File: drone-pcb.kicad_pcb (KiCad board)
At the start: 2 copper layers, 65 x 48.5 mm, 46 parts, among them J1 Conn_01x02_Pin, J10 Conn_01x03_Pin, J11 Conn_01x03_Pin, J12 Conn_01x03_Pin, J2 Conn_01x02_Pin, J3 Conn_01x02_Pin, J4 Conn_01x02_Pin, J5 Conn_01x02_Pin, J6 Conn_01x02_Pin, J7 USB_C_Receptacle_USB2.0_16P, J8 Conn_01x02_Pin, J9 Conn_01x03_Pin, Q1 AO3400A, Q2 AO3400A, Q3 AO3400A, Q4 AO3400A, Q5 AO3400A, Q6 AO3400A, SW1 CK_KMS2xxGP, U1 STM32F030C8Tx, U2 nRF24L01P, U3 MCP73831-2-OT, U4 TLV75533PDBV

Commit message: test export after makefile genaralisation
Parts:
- added U5: MPU-6050, Sensor_Motion:InvenSense_QFN-24_4x4mm_P0.5mm, F.Cu at (142.2, 120.7)
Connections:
- J8 pad 1: /battery+ -> /Vmotor
- R11 pad 1: /m1 -> Net-(Q1-G)
- R12 pad 1: /m2 -> Net-(Q2-G)
- R13 pad 1: /m3 -> Net-(Q3-G)
- R14 pad 1: /m4 -> Net-(Q4-G)
- R15 pad 1: /m5 -> Net-(Q5-G)
- R16 pad 1: /m6 -> Net-(Q6-G)
- U3 pad 3: /battery+ -> /Vmotor
- U4 pad 1: /battery+ -> /Vmotor
- U4 pad 3: /battery+ -> /Vmotor

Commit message: start placing footprints
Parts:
- moved SW1 80.0 mm to (147.6, 42.9)
- moved R13 79.5 mm to (114.6, 34.8)
- moved R12 79.5 mm to (114.6, 31.9)
- moved J3 78.3 mm to (81.6, 45.1), turned to -135 degrees
- moved Q6 77.1 mm to (198.3, 86.2)
- moved R7 76.3 mm to (189.0, 61.6)
- moved J2 69.8 mm to (69.1, 85.8), turned to -90 degrees
- moved Q3 65.9 mm to (89.5, 52.5)
- moved J8 65.0 mm to (102.0, 107.9)
- moved U3 63.8 mm to (111.9, 102.8)
- moved R6 63.5 mm to (191.2, 84.7)
- moved R3 60.1 mm to (96.9, 54.1)
- moved R17 59.7 mm to (161.5, 45.2)
- moved R8 57.7 mm to (188.1, 67.4), turned to 180 degrees
- moved Q4 56.9 mm to (185.2, 114.2)
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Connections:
- U5 pad 1: unconnected-(U5-CLKIN-Pad1) -> GND
- U5 pad 12: unconnected-(U5-INT-Pad12) -> /imu_INT
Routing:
- added copper zone on B.Cu, net GND
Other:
- board outline removed

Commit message: half done
placed chips, not routed, schematic incomplete
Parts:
- removed C4: C, Capacitor_SMD:C_0805_2012Metric_Pad1.18x1.45mm_HandSolder
- removed J11, J12: Conn_01x03_Pin, Connector_PinHeader_2.54mm:PinHeader_1x03_P2.54mm_Vertical
- removed R16: 100k, Resistor_SMD:R_0805_2012Metric_Pad1.20x1.40mm_HandSolder
- removed R17, R18: 10k, Resistor_SMD:R_0805_2012Metric_Pad1.20x1.40mm_HandSolder
- removed R7, R8: 27, Resistor_SMD:R_0805_2012Metric_Pad1.20x1.40mm_HandSolder
- removed SW1: CK_KMS2xxGP, Button_Switch_SMD:SW_SPST_CK_KMS2xxGP
- added D2: LED, LED_SMD:LED_0805_2012Metric_Pad1.15x1.40mm_HandSolder, F.Cu at (203.7, 101.7)
- added REF**: MountingHole_3.2mm_M3_ISO7380, MountingHole:MountingHole_3.2mm_M3_ISO7380, F.Cu at (239.3, 74.9)
- added REF**: MountingHole_3.2mm_M3_ISO7380, MountingHole:MountingHole_3.2mm_M3_ISO7380, F.Cu at (239.2, 105.7)
- added REF**: MountingHole_3.2mm_M3_ISO7380, MountingHole:MountingHole_3.2mm_M3_ISO7380, F.Cu at (205.3, 75.0)
- added REF**: MountingHole_3.2mm_M3_ISO7380, MountingHole:MountingHole_3.2mm_M3_ISO7380, F.Cu at (205.2, 105.7)
- added SW2: SW_Push_Dual_x2, ch32-devBoard-symbols:smd-push-button-TS3425PA, F.Cu at (239.3, 80.1)
- added U6: DW01A, Package_TO_SOT_SMD:SOT-23-6, F.Cu at (204.8, 81.0)
- C1, C2, C3, Q1, Q2, Q3, Q4, Q5, Q6, R11, R12, R3, R4, R5, R6: moved to B.Cu
- J5: value Conn_01x02_Pin -> USB_C_Receptacle_USB2.0_16P; footprint Connector_JST:JST_XH_S2B-XH-A-1_1x02_P2.50mm_Horizontal -> Connector_USB:USB_C_Receptacle_HCTL_HC-TYPE-C-16P-01A
- J6: footprint Connector_JST:JST_XH_S2B-XH-A-1_1x02_P2.50mm_Horizontal -> Connector_JST:JST_XH_B2B-XH-A_1x02_P2.50mm_Vertical
- J7: value USB_C_Receptacle_USB2.0_16P -> Conn_01x03_Pin; footprint Connector_USB:USB_C_Receptacle_HCTL_HC-TYPE-C-16P-01A -> Connector_PinHeader_2.54mm:PinHeader_1x03_P2.54mm_Vertical
- J8: value Conn_01x02_Pin -> Conn_01x03_Pin; footprint Connector_JST:JST_XH_B2B-XH-A_1x02_P2.50mm_Vertical -> Connector_PinHeader_2.54mm:PinHeader_1x03_P2.54mm_Vertical
- R1, R2: value 100R -> 5.1k; moved to B.Cu
- R10, R9: value 4.7k -> 100k; moved to B.Cu
- R13, R14, R15: value 100k -> 10k
- U1: value STM32F030C8Tx -> STM32F103C8Tx
- U2: value nRF24L01P -> TLV75533PDBV; footprint Package_DFN_QFN:QFN-20-1EP_4x4mm_P0.5mm_EP2.5x2.5mm -> Package_TO_SOT_SMD:SOT-23-5
- U3: value MCP73831-2-OT -> MPU-9250; footprint Package_TO_SOT_SMD:SOT-23-5 -> Sensor_Motion:InvenSense_QFN-24_3x3mm_P0.4mm
- U4: value TLV75533PDBV -> MCP73831-2-OT
- U5: value MPU-6050 -> nRF24L01P; footprint Sensor_Motion:InvenSense_QFN-24_4x4mm_P0.5mm -> Package_DFN_QFN:QFN-20-1EP_4x4mm_P0.5mm_EP2.5x2.5mm
- moved J2 171.3 mm to (240.3, 90.2), turned to 90 degrees
- moved Q2 161.3 mm to (236.4, 86.8), turned to 0 degrees
- moved Q3 147.1 mm to (228.2, 101.7), turned to -90 degrees
- moved R2 133.3 mm to (214.5, 105.2), turned to -90 degrees
- moved J9 132.3 mm to (240.4, 95.2)
- moved J8 130.7 mm to (232.6, 101.9)
- moved J3 130.2 mm to (204.0, 89.6), turned to -90 degrees
- moved R3 129.5 mm to (224.3, 77.3), turned to -90 degrees
- moved J10 124.0 mm to (236.7, 95.2)
- moved U3 118.3 mm to (229.7, 91.6)
- moved R13 113.2 mm to (208.3, 98.3)
- moved R11 112.8 mm to (225.4, 101.3), turned to 90 degrees
- moved R12 110.2 mm to (208.0, 90.3)
- moved U5 106.3 mm to (229.7, 82.8)
- moved R1 96.0 mm to (211.0, 105.3)
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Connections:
- J1 pad 1: /Vmotor -> /Vbat
- J10 pad 1: +3V3 -> /swdio
- J10 pad 2: /boot1 -> /swdclk
- J2 pad 1: /Vmotor -> /Vbat
- J3 pad 1: /Vmotor -> /Vbat
- J3 pad 2: /g3 -> /g4
- J4 pad 1: /Vmotor -> /Vbat
- J4 pad 2: /g4 -> /g3
- J6 pad 1: /Vmotor -> /battery+
- J6 pad 2: /g6 -> GND
- J8 pad 1: /Vmotor -> +3V3
- J8 pad 2: GND -> /boot1
- J9 pad 1: +3V3 -> /uart_tx
- J9 pad 2: /boot0 -> /uart_rx
- Q5 pad 1: Net-(Q5-G) -> /charge_gate
- Q5 pad 2: GND -> /battery+
- Q5 pad 3: /g5 -> Net-(Q5-D)
- Q6 pad 1: Net-(Q6-G) -> /discharge_gate
- Q6 pad 2: GND -> /Vbat
- Q6 pad 3: /g6 -> /battery+
- R1 pad 1: Net-(Q1-G) -> Net-(J5-CC1)
- R1 pad 2: /m1 -> GND
- R10 pad 1: Net-(J7-CC2) -> Net-(Q2-G)
- R11 pad 1: Net-(Q1-G) -> Net-(Q3-G)
- R12 pad 1: Net-(Q2-G) -> Net-(Q4-G)
- R13 pad 1: Net-(Q3-G) -> Net-(D1-A)
- R13 pad 2: GND -> /Vbat
- R14 pad 1: Net-(Q4-G) -> /nrst
- R14 pad 2: GND -> +3V3
- R15 pad 1: Net-(Q5-G) -> Net-(D2-A)
- R15 pad 2: GND -> /led
- R2 pad 1: Net-(Q2-G) -> Net-(J5-CC2)
- R2 pad 2: /m2 -> GND
- R3 pad 1: Net-(Q3-G) -> Net-(Q1-G)
- R3 pad 2: /m3 -> /m1
- R4 pad 1: Net-(Q4-G) -> Net-(Q2-G)
- R4 pad 2: /m4 -> /m2
- R5 pad 1: Net-(Q5-G) -> Net-(Q3-G)
- R5 pad 2: /m5 -> /m3
- R6 pad 1: Net-(Q6-G) -> Net-(Q4-G)
- R6 pad 2: /m6 -> /m4
- R9 pad 1: Net-(J7-CC1) -> Net-(Q1-G)
- U1 pad 14: /m6 -> unconnected-(U1-PA4-Pad14)
- U1 pad 15: /m5 -> unconnected-(U1-PA5-Pad15)
- U1 pad 18: unconnected-(U1-PB0-Pad18) -> /led
- U1 pad 20: unconnected-(U1-PB2-Pad20) -> /boot1
- U1 pad 32: unconnected-(U1-PA11-Pad32) -> /d-
- U1 pad 33: unconnected-(U1-PA12-Pad33) -> /d+
- U1 pad 34: unconnected-(U1-PA13-Pad34) -> /swdio
- U1 pad 35: unconnected-(U1-PF6-Pad35) -> GND
- U1 pad 36: unconnected-(U1-PF7-Pad36) -> +3V3
- U1 pad 37: unconnected-(U1-PA14-Pad37) -> /swdclk
- U2 pad 1: unconnected-(U2-CE-Pad1) -> /Vbat
- U2 pad 2: unconnected-(U2-CSN-Pad2) -> GND
- U2 pad 3: unconnected-(U2-SCK-Pad3) -> /Vbat
- U2 pad 5: unconnected-(U2-MISO-Pad5) -> +3V3
- U3 pad 1: /batteryCharging_stat -> unconnected-(U3-RESV_VDDIO-Pad1)
- U3 pad 2: GND -> (no net)
- U3 pad 3: /Vmotor -> (no net)
- U3 pad 4: /Vbus -> (no net)
- U3 pad 5: unconnected-(U3-PROG-Pad5) -> (no net)
- U4 pad 1: /Vmotor -> /batteryCharging_stat
- U4 pad 3: /Vmotor -> Net-(Q5-D)
- U4 pad 4: unconnected-(U4-NC-Pad4) -> /Vbus
- U4 pad 5: +3V3 -> unconnected-(U4-PROG-Pad5)
- U5 pad 1: GND -> unconnected-(U5-CE-Pad1)
- U5 pad 11: unconnected-(U5-FSYNC-Pad11) -> +3V3
- U5 pad 12: /imu_INT -> unconnected-(U5-ANT1-Pad12)
- U5 pad 13: +3V3 -> unconnected-(U5-ANT2-Pad13)
- U5 pad 14: unconnected-(U5-NC-Pad14) -> GND
- U5 pad 15: unconnected-(U5-NC-Pad15) -> +3V3
- U5 pad 17: unconnected-(U5-NC-Pad17) -> GND
- U5 pad 18: GND -> +3V3
- U5 pad 20: unconnected-(U5-CPOUT-Pad20) -> GND
- U5 pad 21: unconnected-(U5-RESV-Pad21) -> (no net)
- U5 pad 7: unconnected-(U5-AUX_CL-Pad7) -> +3V3
- U5 pad 8: unconnected-(U5-VLOGIC-Pad8) -> GND
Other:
- board outline added: 40.3 x 37.1 mm
- board text added: "designed in: Param makers adda"
- board text added: "license: CERN-OHL-W V2.0"
- board text added: "pdr-01"

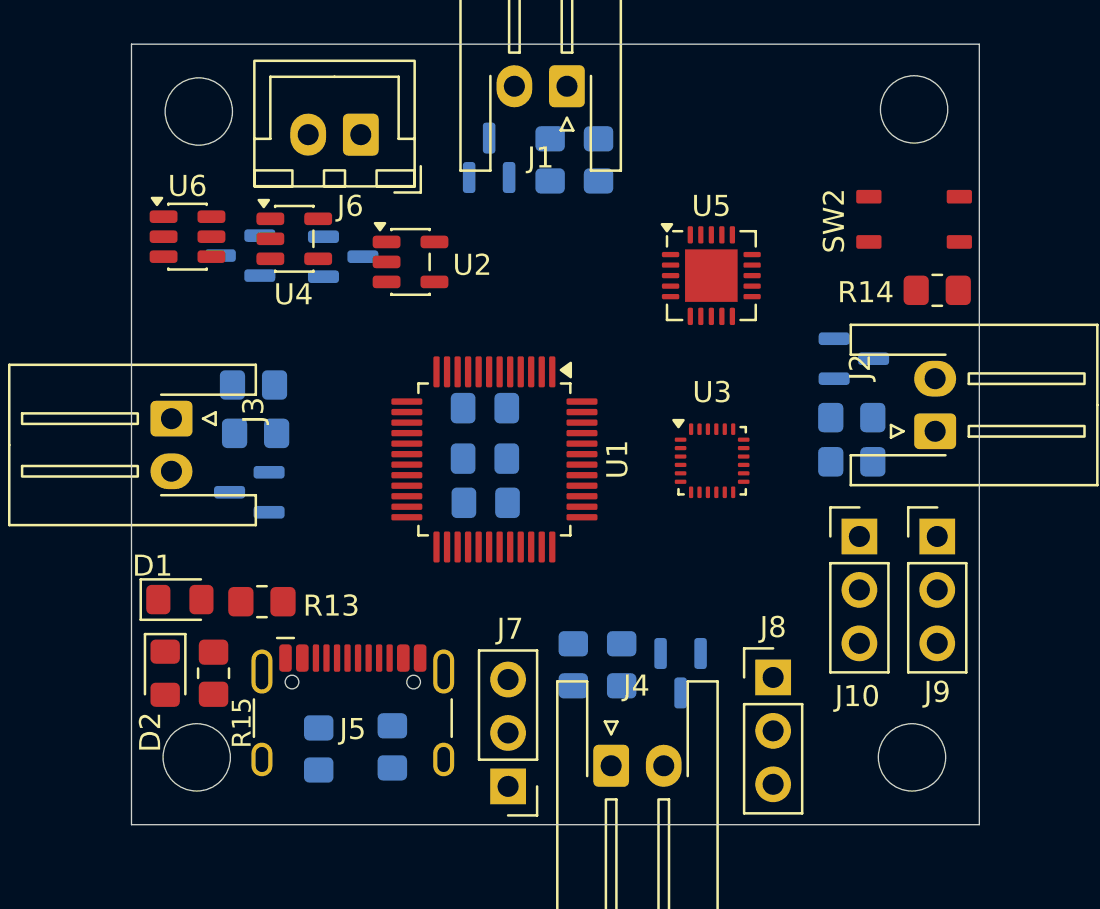
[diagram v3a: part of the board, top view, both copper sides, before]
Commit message: connect nrf24l01+ and mpu6050
add resistor to prog pin in lipo charger, add d+ pullup to the stm32, add input and output voltage capacitors to lipo charger
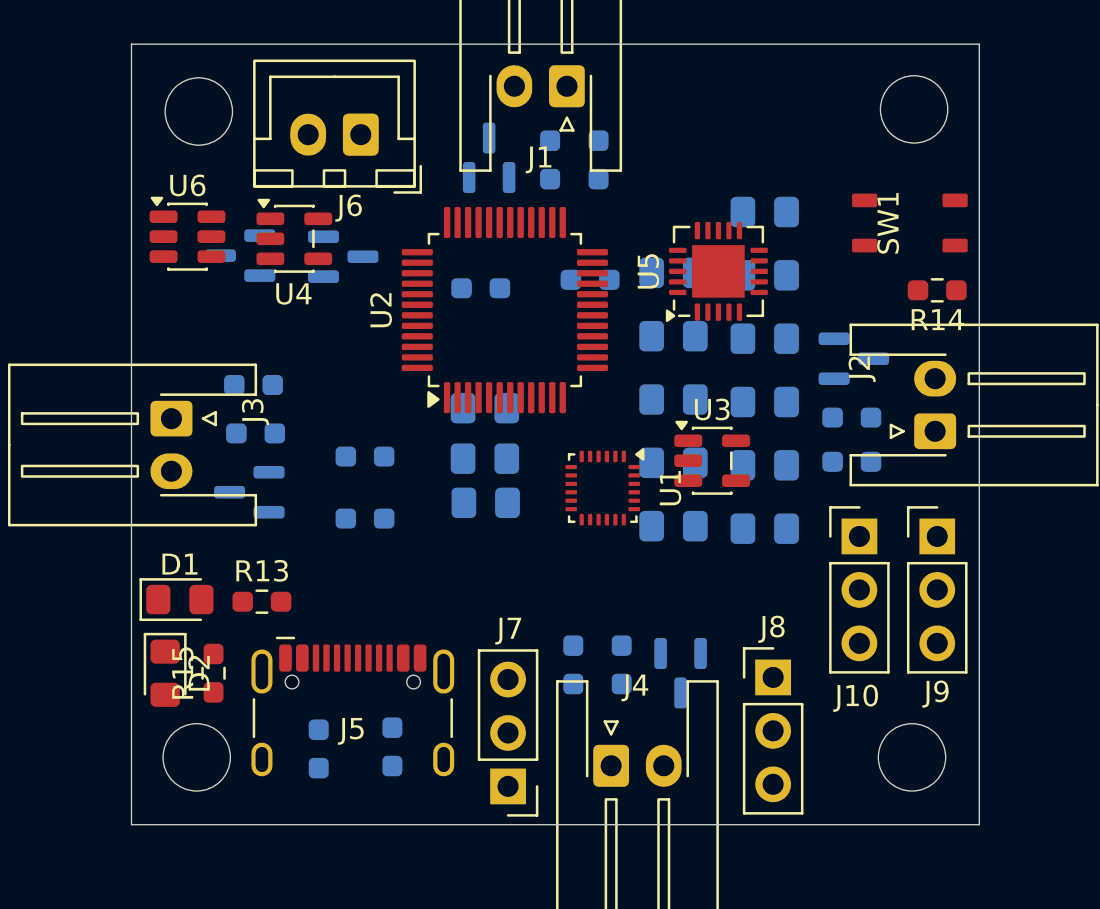
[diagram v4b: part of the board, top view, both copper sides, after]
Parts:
- removed SW2: SW_Push_Dual_x2, ch32-devBoard-symbols:smd-push-button-TS3425PA
- added C10: 100nF, Capacitor_SMD:C_0805_2012Metric_Pad1.18x1.45mm_HandSolder, B.Cu at (227.9, 82.7)
- added C11: 100nF, Capacitor_SMD:C_0805_2012Metric_Pad1.18x1.45mm_HandSolder, B.Cu at (227.9, 85.7)
- added C12: 10nF, Capacitor_SMD:C_0805_2012Metric_Pad1.18x1.45mm_HandSolder, B.Cu at (227.9, 88.7)
- added C13: 4.7uF, Capacitor_SMD:C_0805_2012Metric_Pad1.18x1.45mm_HandSolder, B.Cu at (227.9, 91.7)
- added C14: 4.7uF, Capacitor_SMD:C_0805_2012Metric_Pad1.18x1.45mm_HandSolder, B.Cu at (227.9, 94.7)
- added C4: C, Capacitor_SMD:C_0805_2012Metric_Pad1.18x1.45mm_HandSolder, B.Cu at (232.2, 79.8)
- added C5: 10nF, Capacitor_SMD:C_0805_2012Metric_Pad1.18x1.45mm_HandSolder, B.Cu at (232.2, 82.8)
- added C6: 1nF, Capacitor_SMD:C_0805_2012Metric_Pad1.18x1.45mm_HandSolder, B.Cu at (232.2, 85.8)
- added C7: 33nF, Capacitor_SMD:C_0805_2012Metric_Pad1.18x1.45mm_HandSolder, B.Cu at (232.2, 88.8)
- added C8: 22pF, Capacitor_SMD:C_0805_2012Metric_Pad1.18x1.45mm_HandSolder, B.Cu at (232.2, 91.8)
- added C9: 22pF, Capacitor_SMD:C_0805_2012Metric_Pad1.18x1.45mm_HandSolder, B.Cu at (232.2, 94.8)
- added R16: 10k, Resistor_SMD:R_0603_1608Metric_Pad0.98x0.95mm_HandSolder, B.Cu at (213.2, 91.4)
- added R17: 10k, Resistor_SMD:R_0603_1608Metric_Pad0.98x0.95mm_HandSolder, B.Cu at (213.2, 94.3)
- added R7: 100k, Resistor_SMD:R_0603_1608Metric_Pad0.98x0.95mm_HandSolder, B.Cu at (223.9, 83.0)
- added R8: 100k, Resistor_SMD:R_0603_1608Metric_Pad0.98x0.95mm_HandSolder, B.Cu at (218.7, 83.4)
- added SW1: SW_Push_Dual_x2, ch32-devBoard-symbols:smd-push-button-TS3425PA, F.Cu at (239.1, 80.3)
- R1, R10, R2, R3, R4, R5, R6, R9: footprint Resistor_SMD:R_0805_2012Metric_Pad1.20x1.40mm_HandSolder -> Resistor_SMD:R_0603_1608Metric_Pad0.98x0.95mm_HandSolder
- R11: value 100k -> 10k; footprint Resistor_SMD:R_0805_2012Metric_Pad1.20x1.40mm_HandSolder -> Resistor_SMD:R_0603_1608Metric_Pad0.98x0.95mm_HandSolder
- R12: value 100k -> R; footprint Resistor_SMD:R_0805_2012Metric_Pad1.20x1.40mm_HandSolder -> Resistor_SMD:R_0603_1608Metric_Pad0.98x0.95mm_HandSolder
- R13: value 10k -> R; footprint Resistor_SMD:R_0805_2012Metric_Pad1.20x1.40mm_HandSolder -> Resistor_SMD:R_0603_1608Metric_Pad0.98x0.95mm_HandSolder
- R14: value 10k -> 22K; footprint Resistor_SMD:R_0805_2012Metric_Pad1.20x1.40mm_HandSolder -> Resistor_SMD:R_0603_1608Metric_Pad0.98x0.95mm_HandSolder
- R15: value 10k -> 1M; footprint Resistor_SMD:R_0805_2012Metric_Pad1.20x1.40mm_HandSolder -> Resistor_SMD:R_0603_1608Metric_Pad0.98x0.95mm_HandSolder
- U1: value STM32F103C8Tx -> MPU-9250; footprint Package_QFP:LQFP-48_7x7mm_P0.5mm -> Sensor_Motion:InvenSense_QFN-24_3x3mm_P0.4mm
- U2: value TLV75533PDBV -> STM32F103C8Tx; footprint Package_TO_SOT_SMD:SOT-23-5 -> Package_QFP:LQFP-48_7x7mm_P0.5mm
- U3: value MPU-9250 -> TLV75533PDBV; footprint Sensor_Motion:InvenSense_QFN-24_3x3mm_P0.4mm -> Package_TO_SOT_SMD:SOT-23-5
- moved U1 5.33 mm to (224.5, 92.9)
- moved U2 5.04 mm to (219.8, 84.4), turned to 90 degrees
- moved U5 0.39 mm to (230.0, 82.6), turned to 90 degrees
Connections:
- C3 pad 1: +3V3 -> /OSC_IN
- Q5 pad 2: /battery+ -> /Vbat
- R10 pad 1: Net-(Q2-G) -> Net-(Q4-G)
- R11 pad 1: Net-(Q3-G) -> Net-(D1-A)
- R11 pad 2: GND -> /Vbat
- R12 pad 1: Net-(Q4-G) -> +3V3
- R12 pad 2: GND -> /radio_SPI_CSN
- R13 pad 1: Net-(D1-A) -> GND
- R13 pad 2: /Vbat -> /radio_enable
- R14 pad 1: /nrst -> GND
- R14 pad 2: +3V3 -> Net-(U5-IREF)
- R15 pad 1: Net-(D2-A) -> /radio_XC1
- R15 pad 2: /led -> /radio_XC2
- R9 pad 1: Net-(Q1-G) -> Net-(Q3-G)
- U1 pad 10: /m1 -> /imu_regout
- U1 pad 11: /m2 -> GND
- U1 pad 12: /m3 -> /imu_int
- U1 pad 13: /m4 -> +3V3
- U1 pad 14: unconnected-(U1-PA4-Pad14) -> (no net)
- U1 pad 15: unconnected-(U1-PA5-Pad15) -> (no net)
- U1 pad 16: unconnected-(U1-PA6-Pad16) -> (no net)
- U1 pad 17: unconnected-(U1-PA7-Pad17) -> (no net)
- U1 pad 18: /led -> GND
- U1 pad 19: unconnected-(U1-PB1-Pad19) -> (no net)
- U1 pad 2: unconnected-(U1-PC13-Pad2) -> (no net)
- U1 pad 20: /boot1 -> GND
- U1 pad 22: unconnected-(U1-PB11-Pad22) -> /imu_spi_cs
- U1 pad 23: GND -> /imu_spi_clk
- U1 pad 24: +3V3 -> /imu_mosi
- U1 pad 3: unconnected-(U1-PC14-Pad3) -> (no net)
- U1 pad 4: unconnected-(U1-PC15-Pad4) -> (no net)
- U1 pad 5: unconnected-(U1-PD0-Pad5) -> (no net)
- U1 pad 6: unconnected-(U1-PD1-Pad6) -> (no net)
- U1 pad 7: /nrst -> unconnected-(U1-AUX_CL-Pad7)
- U1 pad 8: GND -> +3V3
- U1 pad 9: +3V3 -> /imu_miso
- U2 pad 1: /Vbat -> +3V3
- U2 pad 2: GND -> unconnected-(U2-PC13-Pad2)
- U2 pad 3: /Vbat -> unconnected-(U2-PC14-Pad3)
- U2 pad 5: +3V3 -> /OSC_IN
- U3 pad 1: unconnected-(U3-RESV_VDDIO-Pad1) -> /Vbat
- U3 pad 2: (no net) -> GND
- U3 pad 3: (no net) -> /Vbat
- U3 pad 4: (no net) -> unconnected-(U3-NC-Pad4)
- U3 pad 5: (no net) -> +3V3
- U4 pad 5: unconnected-(U4-PROG-Pad5) -> Net-(U4-PROG)
- U5 pad 1: unconnected-(U5-CE-Pad1) -> /radio_enable
- U5 pad 10: unconnected-(U5-XC1-Pad10) -> /radio_XC1
- U5 pad 16: unconnected-(U5-IREF-Pad16) -> Net-(U5-IREF)
- U5 pad 19: unconnected-(U5-DVDD-Pad19) -> Net-(U5-DVDD)
- U5 pad 2: unconnected-(U5-CSN-Pad2) -> /radio_SPI_CSN
- U5 pad 3: unconnected-(U5-SCK-Pad3) -> /radio_SCK
- U5 pad 4: unconnected-(U5-MOSI-Pad4) -> /radio_MOSI
- U5 pad 5: unconnected-(U5-MISO-Pad5) -> /radio_MISO
- U5 pad 6: unconnected-(U5-IRQ-Pad6) -> /radio_IRQ
- U5 pad 9: unconnected-(U5-XC2-Pad9) -> /radio_XC2
